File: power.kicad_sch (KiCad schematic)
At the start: 22 parts, among them IC1 RT8096AHGJ5, IC2 TLV61070A, Q1 SSM3J35AMFV

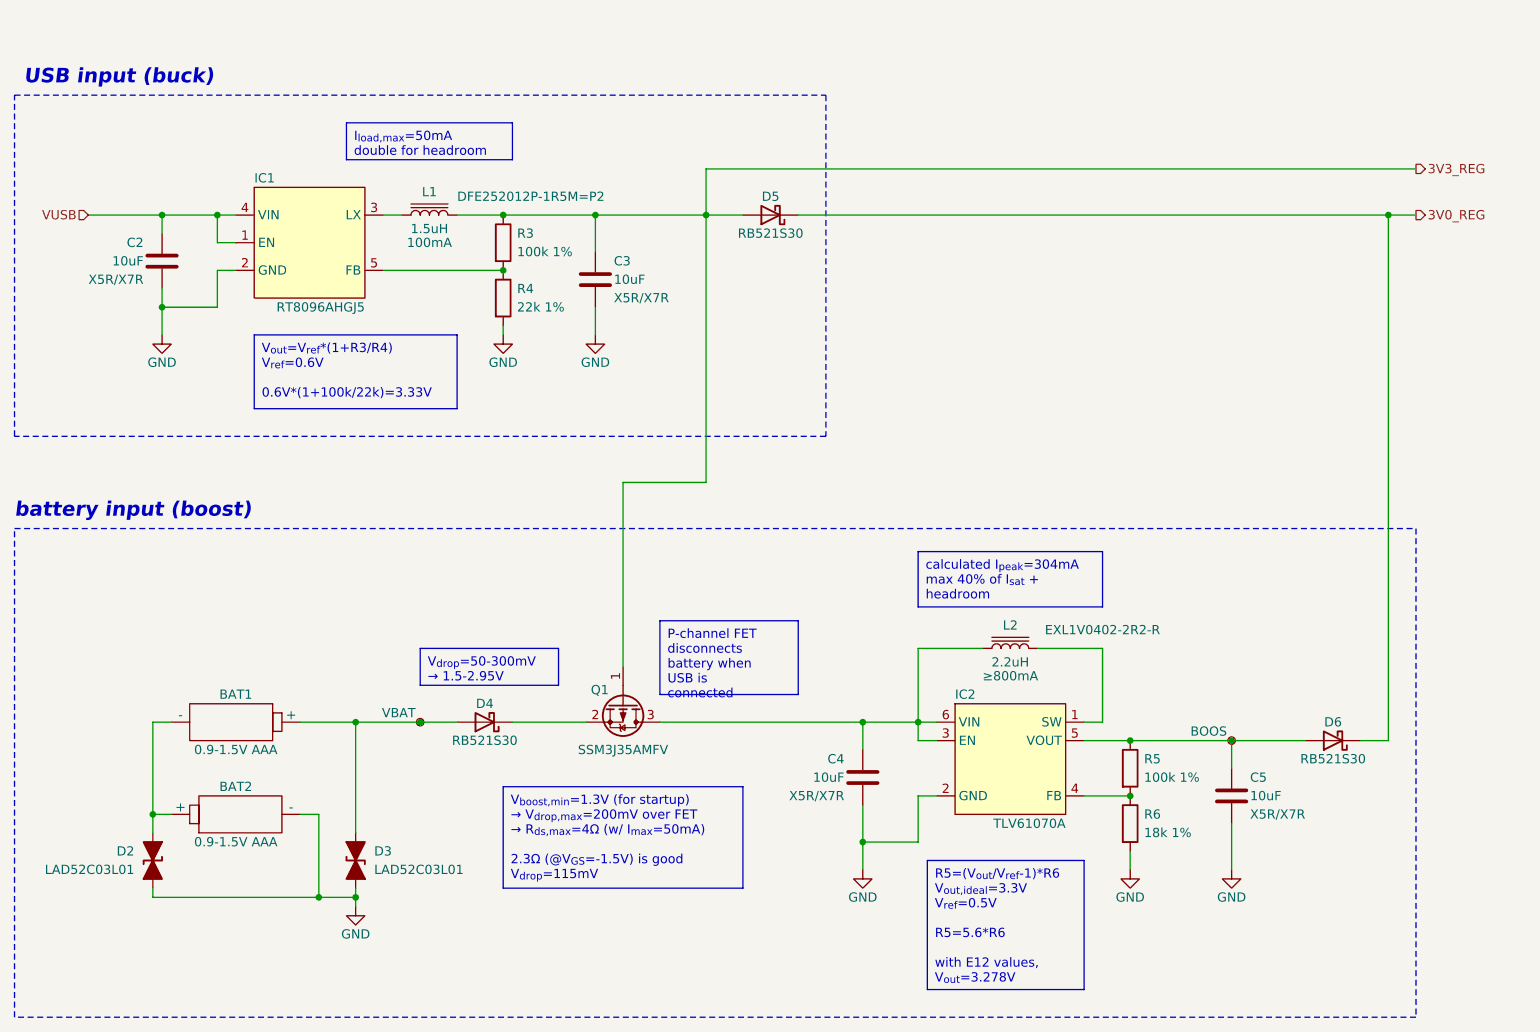
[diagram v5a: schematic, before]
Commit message: add one more battery TVS
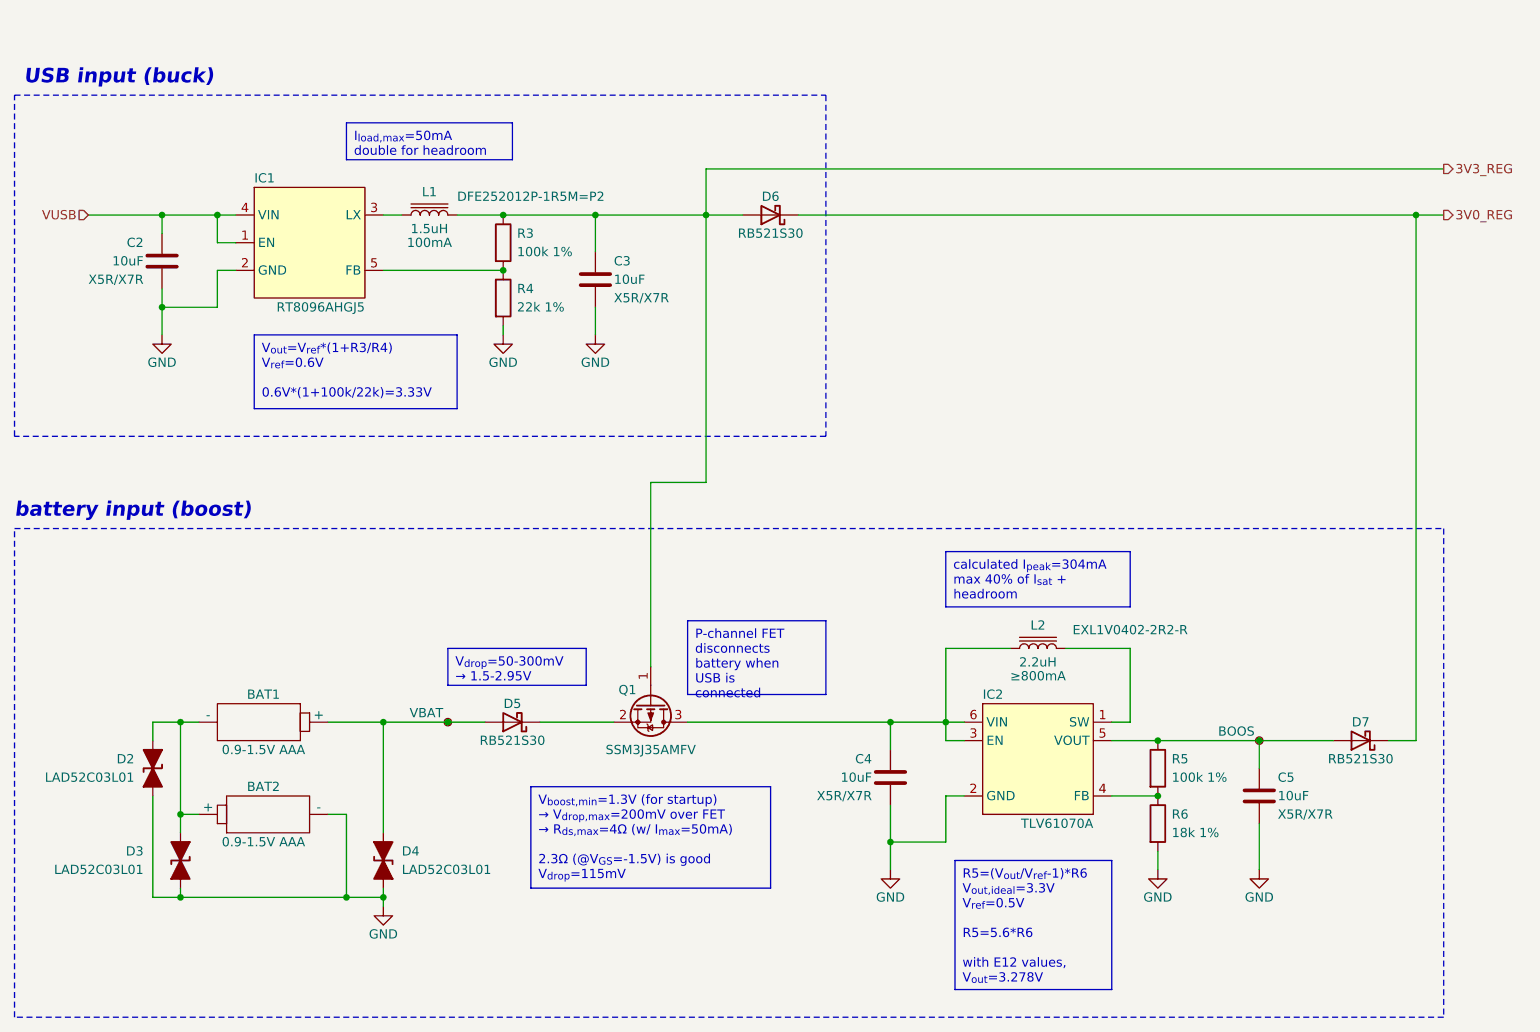
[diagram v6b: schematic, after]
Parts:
- added D2: LAD52C03L01, Diode_SMD:D_SOD-523, symbol Device:D_TVS_Filled
- renumbered D2 to D3, D3 to D4, D4 to D5, D5 to D6, D6 to D7
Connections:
- net GND: now also D2.1 (A1)
- net at BAT1.2 (-), BAT2.1 (+), D3.2 (A2): now also D2.2 (A2)
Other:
- moved on the sheet: BAT1, BAT2, C4, C5, D3, D4, D5, D7, IC2, L2, Q1, R5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

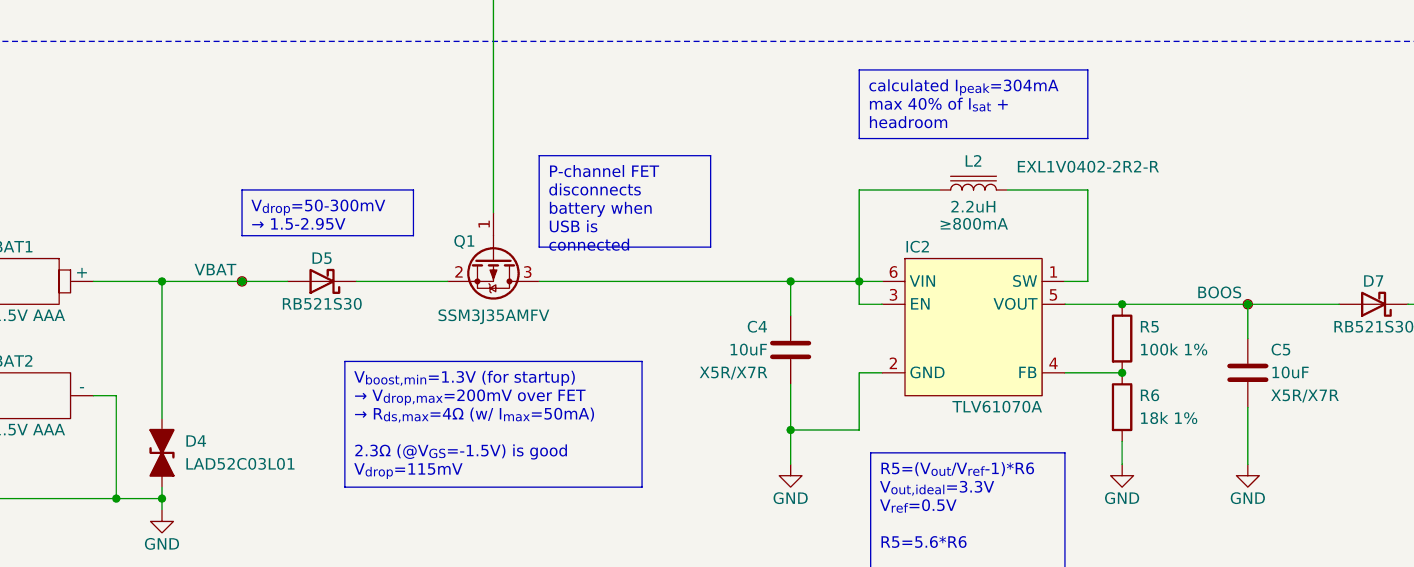
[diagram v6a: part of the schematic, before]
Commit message: pcb done, also kicad 8
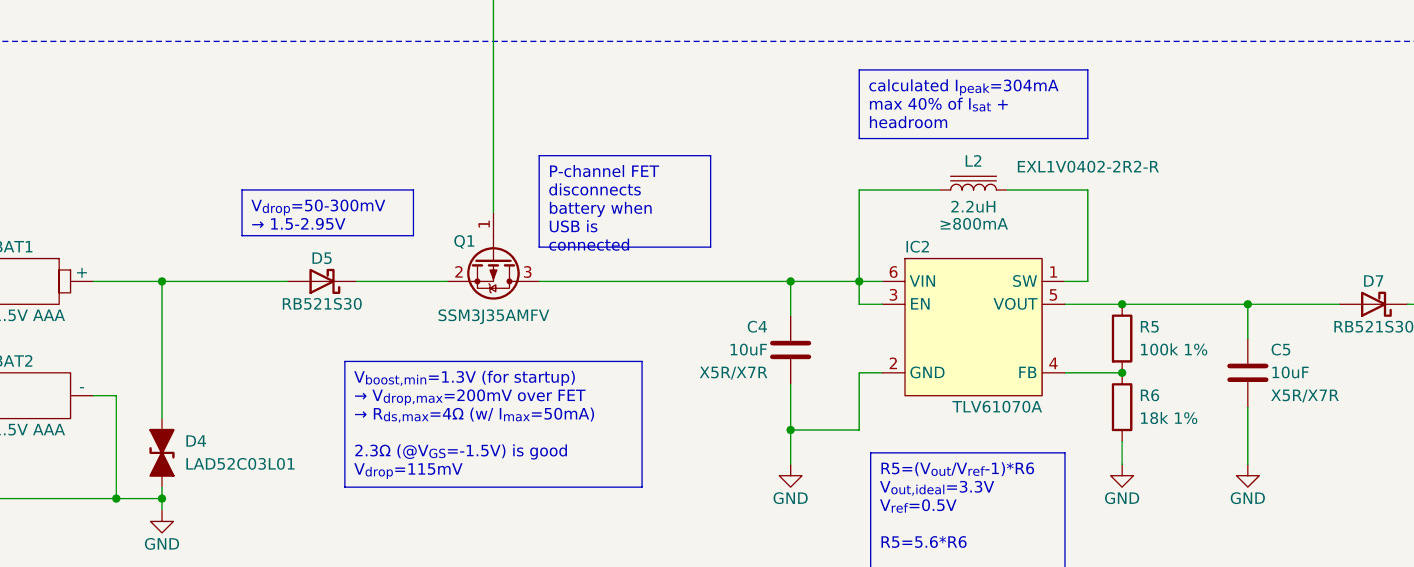
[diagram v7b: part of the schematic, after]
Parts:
- removed TP26: VBAT, TestPoint:TestPoint_Pad_D1.0mm, symbol Connector:TestPoint_Small
- removed TP27: BOOS, TestPoint:TestPoint_Pad_D1.0mm, symbol Connector:TestPoint_Small
